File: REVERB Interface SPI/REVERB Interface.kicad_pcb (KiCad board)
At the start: 2 copper layers, 90.2 x 95.9 mm, 58 parts, among them J1 RPiZeroW, J2 Iridium, J3 APRS, J4 Antenna, M1 MountingHole_Pad, M2 MountingHole_Pad, M3 MountingHole_Pad, M4 MountingHole_Pad, M5 PiMount, M6 PiMount, M7 PiMount, M8 PiMount, U1 LSM9DS1BOB, U2 MAX3232, U3 SC16IS752IPW, Y1 1.8432MHz

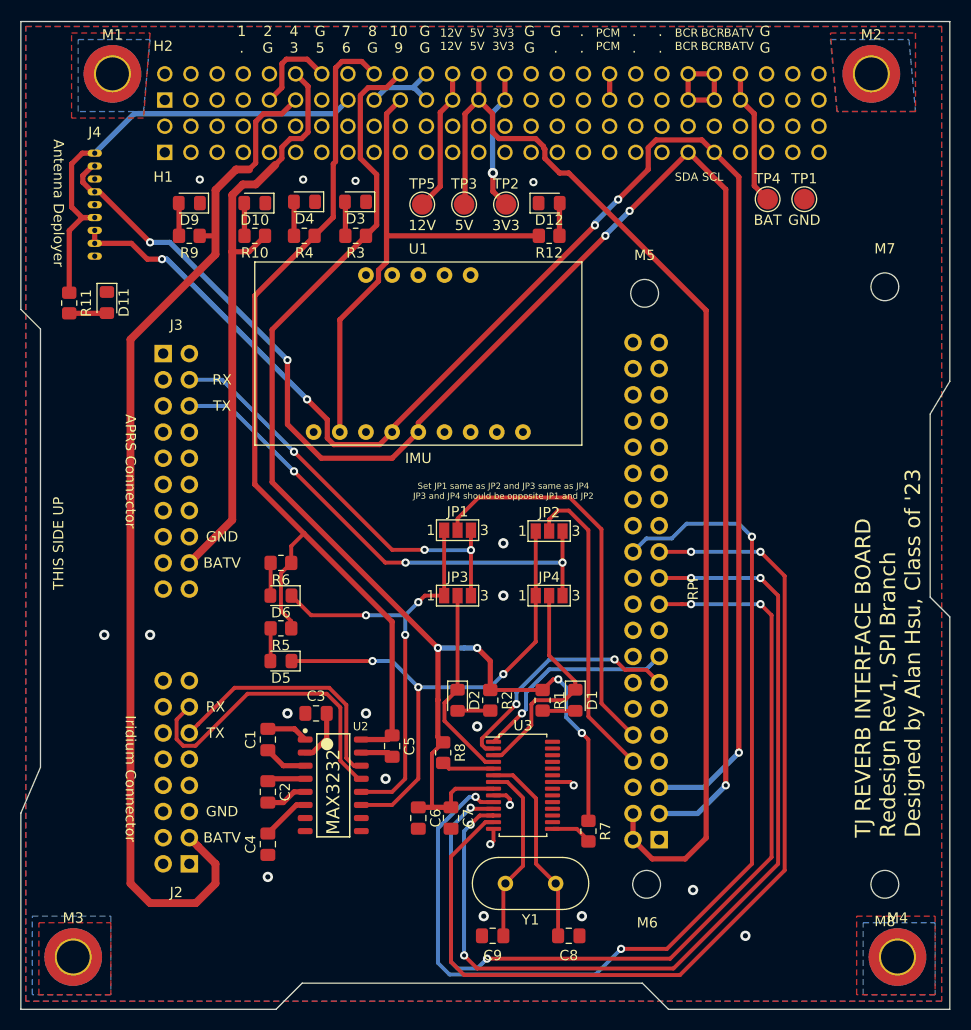
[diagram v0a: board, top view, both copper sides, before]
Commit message: EMI and SI minmaxing, round 2
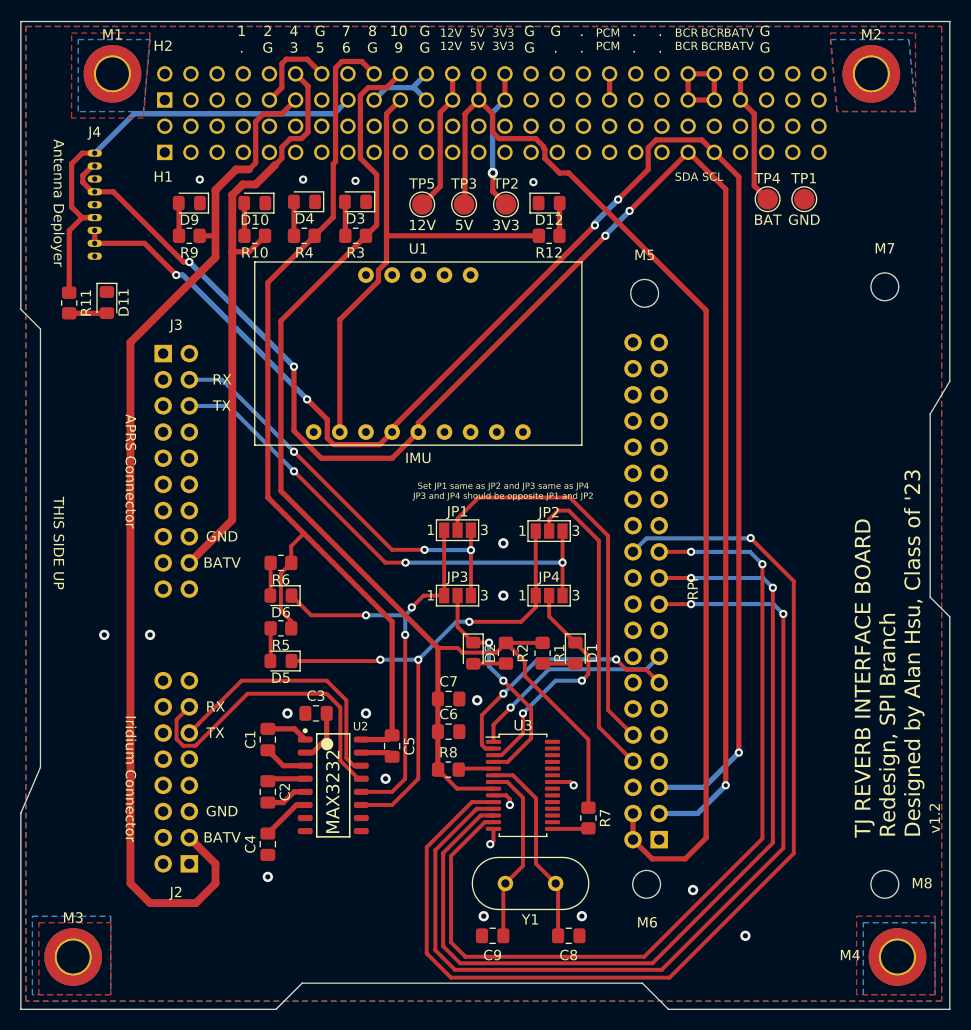
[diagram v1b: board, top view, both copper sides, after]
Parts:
- moved C7 11.6 mm to (148.4, 118.6), turned to 0 degrees
- moved C6 8.88 mm to (148.4, 121.8), turned to 0 degrees
- moved D2 4.82 mm to (150.7, 114.2)
- moved R2 4.82 mm to (153.9, 114.2)
- moved D1 4.57 mm to (160.7, 114.2)
- moved R1 4.57 mm to (157.5, 114.2)
- moved R8 1.73 mm to (148.3, 125.5), turned to 0 degrees
- moved R7 1.27 mm to (161.9, 130.2)
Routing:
- net /SPISCK: track 94.6 -> 86.6 mm
- net /SW10: track 125.5 -> 117.9 mm, vias 4 -> 0
- net /SPICE0: track 100.3 -> 104.5 mm, vias 3 -> 1
- net /SPIUARTRX: track 19.1 -> 22.3 mm, vias 0 -> 2
- net /SPIMOSI: track 88.7 -> 91.7 mm, vias 4 -> 2
- net Net-(R8-Pad2): track 5.11 -> 3.42 mm
- net /T1IN: track 52.8 -> 51.4 mm
- net /SW8: track 91.8 -> 90.7 mm
- net /SPIUARTTX: track 22.0 -> 22.8 mm, vias 0 -> 2
- net /T1OUT: track 24.7 -> 25.5 mm
- net /CTS: track 23.9 -> 24.5 mm
- net /SPIMISO: track 89.1 -> 89.2 mm, vias 4 -> 2
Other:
- board text added: "TJ REVERB INTERFACE BOARD Redesign, SPI Branch Designed by Alan Hsu, Class of '23"
- board text added: "v1.2"
- board text removed: "TJ REVERB INTERFACE BOARD Redesign Rev1, SPI Branch Designed by Alan Hsu, Class of '23"

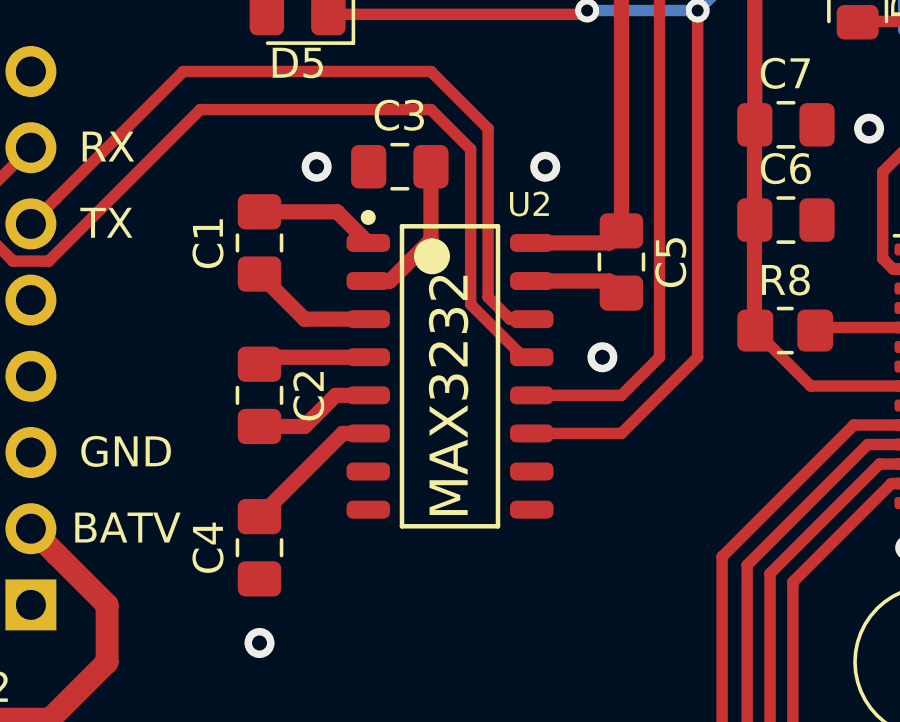
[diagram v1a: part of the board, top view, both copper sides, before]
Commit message: Replace max3232 footprint, update stencil
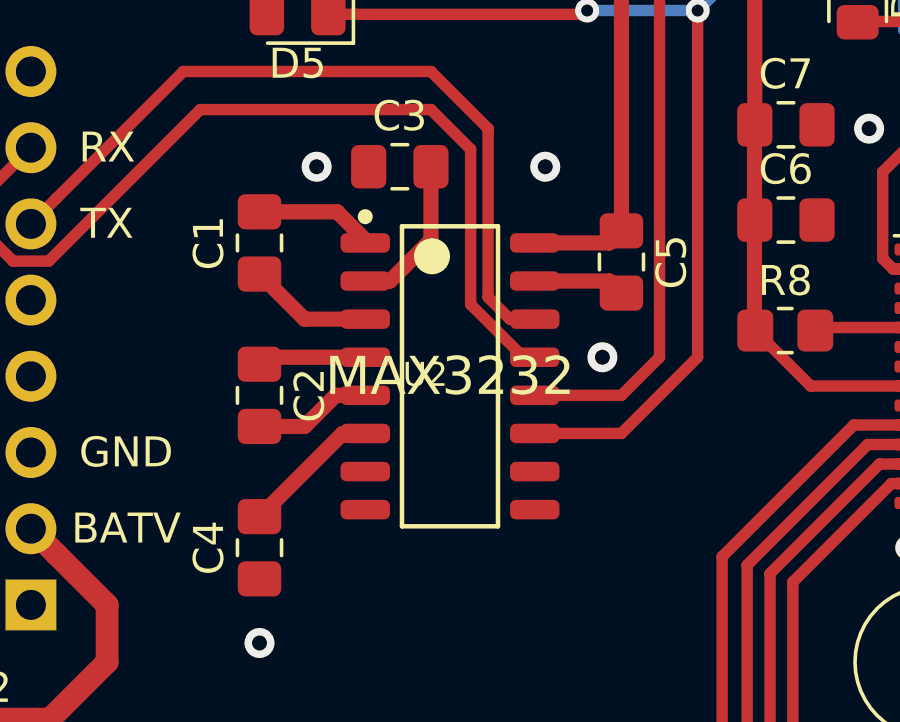
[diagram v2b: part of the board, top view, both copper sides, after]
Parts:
- U2: footprint REVERB Interface:Texas_Instruments-MAX3232ID -> REVERB Interface:Texas_Instruments-MAX3232ID-Level_A
